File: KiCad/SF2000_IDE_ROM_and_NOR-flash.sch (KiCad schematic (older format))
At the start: 3 parts, among them J5 IDE_ATA_44pin, U13 SST39LF040, U14 SST39LF802C

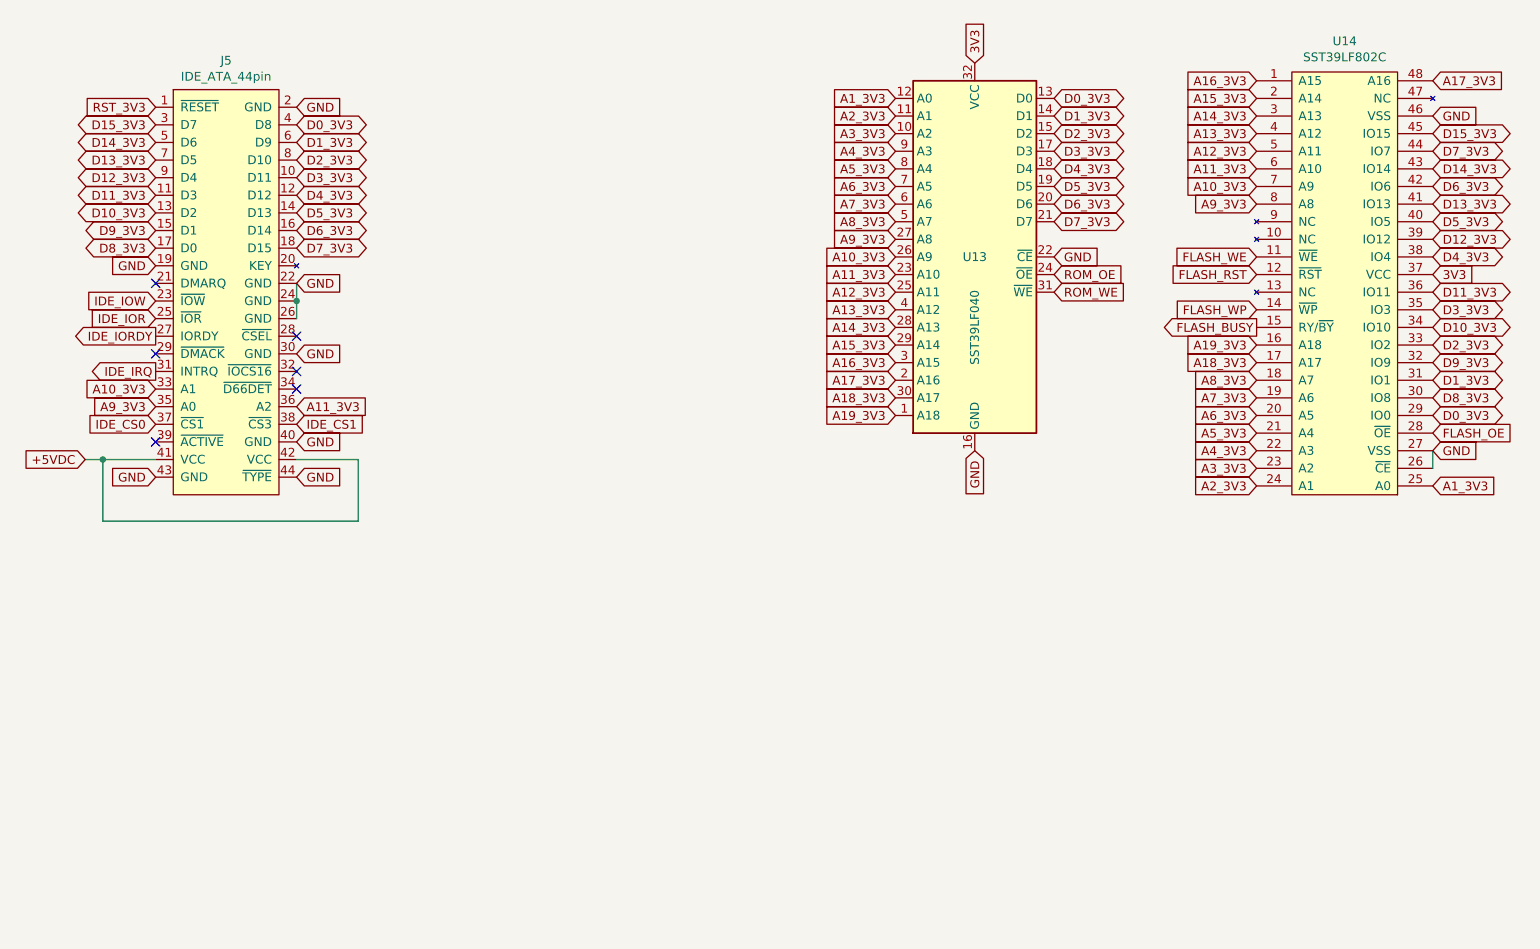
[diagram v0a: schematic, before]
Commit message: added buffering for IDE, rearranged components a bit and did more routing
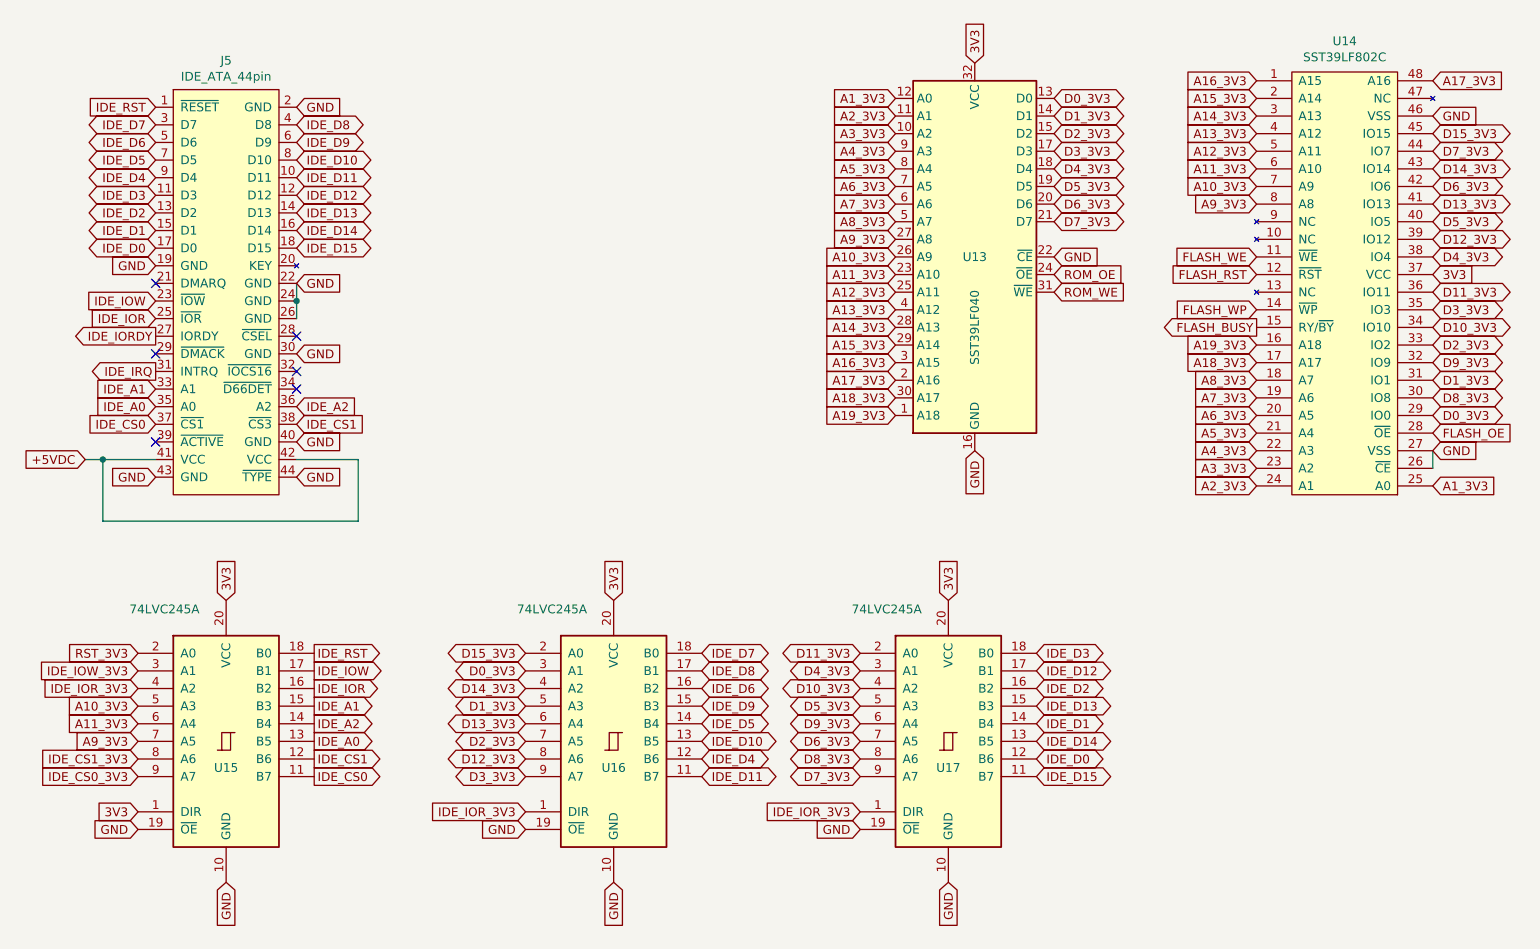
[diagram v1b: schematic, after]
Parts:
- added U15, U16, U17: 74LVC245A, Package_SO:TSSOP-20_4.4x6.5mm_P0.65mm, symbol SF2000:74LVC245A
- J5: footprint Connector_PinSocket_2.00mm:PinSocket_2x22_P2.00mm_Horizontal -> SF2000:PinHeader_2x22_P2.00mm_Vertical
- U13: footprint Package_LCC:PLCC-32_11.4x14.0mm_P1.27mm -> SF2000:PLCC-32_11.4x14.0mm_P1.27mm
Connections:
- net 3V3: now also U15.1 (DIR), U15.20 (VCC), U16.20 (VCC), U17.20 (VCC)
- net A10_3V3: now also U15.5 (A3); no longer J5.33 (A1)
- net A11_3V3: now also U15.6 (A4); no longer J5.36 (A2)
- net A9_3V3: now also U15.7 (A5); no longer J5.35 (A0)
- net D0_3V3: now also U16.3 (A1); no longer J5.4 (D8)
- net D10_3V3: now also U17.4 (A2); no longer J5.13 (D2)
- net D11_3V3: now also U17.2 (A0); no longer J5.11 (D3)
- net D12_3V3: now also U16.8 (A6); no longer J5.9 (D4)
- net D13_3V3: now also U16.6 (A4); no longer J5.7 (D5)
- net D14_3V3: now also U16.4 (A2); no longer J5.5 (D6)
- net D15_3V3: now also U16.2 (A0); no longer J5.3 (D7)
- net D1_3V3: now also U16.5 (A3); no longer J5.6 (D9)
- net D2_3V3: now also U16.7 (A5); no longer J5.8 (D10)
- net D3_3V3: now also U16.9 (A7); no longer J5.10 (D11)
- net D4_3V3: now also U17.3 (A1); no longer J5.12 (D12)
- net D5_3V3: now also U17.5 (A3); no longer J5.14 (D13)
- net D6_3V3: now also U17.7 (A5); no longer J5.16 (D14)
- net D7_3V3: now also U17.9 (A7); no longer J5.18 (D15)
- net D8_3V3: now also U17.8 (A6); no longer J5.17 (D0)
- net D9_3V3: now also U17.6 (A4); no longer J5.15 (D1)
- net GND: now also U15.10 (GND), U15.19 (~OE), U16.10 (GND), U16.19 (~OE), U17.10 (GND), U17.19 (~OE)
- net IDE_CS0: now also U15.11 (B7)
- net IDE_CS1: now also U15.12 (B6)
- net IDE_IOR: now also U15.16 (B2)
- net IDE_IOW: now also U15.17 (B1)
- net RST_3V3: now also U15.2 (A0); no longer J5.1 (~RESET)
- new net IDE_A0: J5.35 (A0), U15.13 (B5)
- new net IDE_A1: J5.33 (A1), U15.15 (B3)
- new net IDE_A2: J5.36 (A2), U15.14 (B4)
- new net IDE_CS0_3V3: U15.9 (A7)
- new net IDE_CS1_3V3: U15.8 (A6)
- new net IDE_D0: J5.17 (D0), U17.12 (B6)
- new net IDE_D1: J5.15 (D1), U17.14 (B4)
- new net IDE_D10: J5.8 (D10), U16.13 (B5)
- new net IDE_D11: J5.10 (D11), U16.11 (B7)
- new net IDE_D12: J5.12 (D12), U17.17 (B1)
- new net IDE_D13: J5.14 (D13), U17.15 (B3)
- new net IDE_D14: J5.16 (D14), U17.13 (B5)
- new net IDE_D15: J5.18 (D15), U17.11 (B7)
- new net IDE_D2: J5.13 (D2), U17.16 (B2)
- new net IDE_D3: J5.11 (D3), U17.18 (B0)
- new net IDE_D4: J5.9 (D4), U16.12 (B6)
- new net IDE_D5: J5.7 (D5), U16.14 (B4)
- new net IDE_D6: J5.5 (D6), U16.16 (B2)
- new net IDE_D7: J5.3 (D7), U16.18 (B0)
- new net IDE_D8: J5.4 (D8), U16.17 (B1)
- new net IDE_D9: J5.6 (D9), U16.15 (B3)
- new net IDE_IOR_3V3: U15.4 (A2), U16.1 (DIR), U17.1 (DIR)
- new net IDE_IOW_3V3: U15.3 (A1)
- new net IDE_RST: J5.1 (~RESET), U15.18 (B0)
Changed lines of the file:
@@
 F 0 "J5" H 2700 4015 50  0000 C CNN
 F 1 "IDE_ATA_44pin" H 2700 3924 50  0000 C CNN
-F 2 "Connector_PinSocket_2.00mm:PinSocket_2x22_P2.00mm_Horizontal" H 2700 2800 50  0001 C CNN
+F 2 "SF2000:PinHeader_2x22_P2.00mm_Vertical" H 2700 2800 50  0001 C CNN
 F 3 "" H 2700 2800 50  0001 C CNN
 	1    2700 2750
@@
 F 0 "U13" H 6950 2600 50  0000 C CNN
 F 1 "SST39LF040" V 6950 2200 50  0000 C CNN
-F 2 "Package_LCC:PLCC-32_11.4x14.0mm_P1.27mm" H 6950 2600 50  0001 C CNN
+F 2 "SF2000:PLCC-32_11.4x14.0mm_P1.27mm" H 6950 2600 50  0001 C CNN
 F 3 "https://ww1.microchip.com/downloads/en/DeviceDoc/20005023B.pdf" H 6950 2700 50  0001 C CNN
 	1    6950 2600
@@
 Text GLabel 7400 2400 2    50   BiDi ~ 0
 D7_3V3
-Text GLabel 3100 1850 2    50   BiDi ~ 0
+Text GLabel 4400 4950 0    50   BiDi ~ 0
 D0_3V3
-Text GLabel 3100 1950 2    50   BiDi ~ 0
+Text GLabel 4400 5150 0    50   BiDi ~ 0
 D1_3V3
-Text GLabel 3100 2050 2    50   BiDi ~ 0
+Text GLabel 4400 5350 0    50   BiDi ~ 0
 D2_3V3
-Text GLabel 3100 2150 2    50   BiDi ~ 0
+Text GLabel 4400 5550 0    50   BiDi ~ 0
 D3_3V3
-Text GLabel 3100 2250 2    50   BiDi ~ 0
+Text GLabel 6300 4950 0    50   BiDi ~ 0
 D4_3V3
-Text GLabel 3100 2350 2    50   BiDi ~ 0
+Text GLabel 6300 5150 0    50   BiDi ~ 0
 D5_3V3
-Text GLabel 3100 2450 2    50   BiDi ~ 0
+Text GLabel 6300 5350 0    50   BiDi ~ 0
 D6_3V3
-Text GLabel 3100 2550 2    50   BiDi ~ 0
+Text GLabel 6300 5550 0    50   BiDi ~ 0
 D7_3V3
-Text GLabel 2300 2550 0    50   BiDi ~ 0
+Text GLabel 6300 5450 0    50   BiDi ~ 0
 D8_3V3
-Text GLabel 2300 2450 0    50   BiDi ~ 0
+Text GLabel 6300 5250 0    50   BiDi ~ 0
 D9_3V3
-Text GLabel 2300 2350 0    50   BiDi ~ 0
+Text GLabel 6300 5050 0    50   BiDi ~ 0
 D10_3V3
-Text GLabel 2300 2250 0    50   BiDi ~ 0
+Text GLabel 6300 4850 0    50   BiDi ~ 0
 D11_3V3
-Text GLabel 2300 2150 0    50   BiDi ~ 0
+Text GLabel 4400 5450 0    50   BiDi ~ 0
 D12_3V3
-Text GLabel 2300 2050 0    50   BiDi ~ 0
+Text GLabel 4400 5250 0    50   BiDi ~ 0
 D13_3V3
-Text GLabel 2300 1950 0    50   BiDi ~ 0
+Text GLabel 4400 5050 0    50   BiDi ~ 0
 D14_3V3
-Text GLabel 2300 1850 0    50   BiDi ~ 0
+Text GLabel 4400 4850 0    50   BiDi ~ 0
 D15_3V3
-Text GLabel 2300 1750 0    50   Input ~ 0
+Text GLabel 2200 4850 0    50   Input ~ 0
 RST_3V3
 Text GLabel 2300 2650 0    50   Input ~ 0
@@
 Text GLabel 2300 3250 0    50   Output ~ 0
 IDE_IRQ
-Text GLabel 2300 3350 0    50   Input ~ 0
+Text GLabel 2200 5150 0    50   Input ~ 0
 A10_3V3
-Text GLabel 2300 3450 0    50   Input ~ 0
+Text GLabel 2200 5350 0    50   Input ~ 0
 A9_3V3
-Text GLabel 3100 3450 2    50   Input ~ 0
+Text GLabel 2200 5250 0    50   Input ~ 0
 A11_3V3
 Text GLabel 3100 3150 2    50   Input ~ 0
@@
 NoConn ~ 3100 3250
 NoConn ~ 3100 3350
+$Comp
+L SF2000:74LVC245A U15
+U 1 1 628D607F
+P 2700 5350
+F 0 "U15" H 2700 5200 50  0000 C CNN
+F 1 "74LVC245A" H 2350 6100 50  0000 C CNN
+F 2 "Package_SO:TSSOP-20_4.4x6.5mm_P0.65mm" H 2700 5350 50  0001 C CNN
+F 3 "http://www.ti.com/lit/gpn/sn74HC245" H 2700 5350 50  0001 C CNN
+	1    2700 5350
+	1    0    0    -1
+$EndComp
+Text GLabel 2700 4550 1    50   Input ~ 0
+3V3
+Text GLabel 2700 6150 3    50   Input ~ 0
+GND
+Text GLabel 2200 5750 0    50   Input ~ 0
+3V3
+Text GLabel 2200 5850 0    50   Input ~ 0
+GND
+Text GLabel 3200 4850 2    50   Output ~ 0
+IDE_RST
+Text GLabel 2300 1750 0    50   Input ~ 0
+IDE_RST
+Text GLabel 2200 4950 0    50   Input ~ 0
+IDE_IOW_3V3
+Text GLabel 3200 4950 2    50   Output ~ 0
+IDE_IOW
+Text GLabel 2200 5050 0    50   Input ~ 0
+IDE_IOR_3V3
+Text GLabel 3200 5050 2    50   Output ~ 0
+IDE_IOR
+Text GLabel 3200 5150 2    50   Output ~ 0
+IDE_A1
+Text GLabel 2300 3350 0    50   Input ~ 0
+IDE_A1
+Text GLabel 3200 5250 2    50   Output ~ 0
+IDE_A2
+Text GLabel 3200 5350 2    50   Output ~ 0
+IDE_A0
+Text GLabel 3100 3450 2    50   Input ~ 0
+IDE_A2
+Text GLabel 2300 3450 0    50   Input ~ 0
+IDE_A0
+Text GLabel 2200 5450 0    50   Input ~ 0
+IDE_CS1_3V3
+Text GLabel 3200 5450 2    50   Output ~ 0
+IDE_CS1
+Text GLabel 2200 5550 0    50   Input ~ 0
+IDE_CS0_3V3
+Text GLabel 3200 5550 2    50   Output ~ 0
+IDE_CS0
+$Comp
+L SF2000:74LVC245A U16
+U 1 1 628E9EE2
+P 4900 5350
+F 0 "U16" H 4900 5200 50  0000 C CNN
+F 1 "74LVC245A" H 4550 6100 50  0000 C CNN
+F 2 "Package_SO:TSSOP-20_4.4x6.5mm_P0.65mm" H 4900 5350 50  0001 C CNN
+F 3 "http://www.ti.com/lit/gpn/sn74HC245" H 4900 5350 50  0001 C CNN
+	1    4900 5350
+	1    0    0    -1
+$EndComp
+Text GLabel 4900 4550 1    50   Input ~ 0
+3V3
+Text GLabel 4900 6150 3    50   Input ~ 0
+GND
+Text GLabel 4400 5850 0    50   Input ~ 0
+GND
+$Comp
+L SF2000:74LVC245A U17
+U 1 1 628ED6C8
+P 6800 5350
+F 0 "U17" H 6800 5200 50  0000 C CNN
+F 1 "74LVC245A" H 6450 6100 50  0000 C CNN
+F 2 "Package_SO:TSSOP-20_4.4x6.5mm_P0.65mm" H 6800 5350 50  0001 C CNN
+F 3 "http://www.ti.com/lit/gpn/sn74HC245" H 6800 5350 50  0001 C CNN
+	1    6800 5350
+	1    0    0    -1
+$EndComp
+Text GLabel 6800 4550 1    50   Input ~ 0
+3V3
+Text GLabel 6800 6150 3    50   Input ~ 0
+GND
+Text GLabel 6300 5850 0    50   Input ~ 0
+GND
+Text GLabel 6300 5750 0    50   Input ~ 0
+IDE_IOR_3V3
+Text GLabel 4400 5750 0    50   Input ~ 0
+IDE_IOR_3V3
+Text GLabel 5400 4850 2    50   BiDi ~ 0
+IDE_D7
+Text GLabel 2300 1850 0    50   BiDi ~ 0
+IDE_D7
+Text GLabel 5400 4950 2    50   BiDi ~ 0
+IDE_D8
+Text GLabel 3100 1850 2    50   BiDi ~ 0
+IDE_D8
+Text GLabel 5400 5050 2    50   BiDi ~ 0
+IDE_D6
+Text GLabel 2300 1950 0    50   BiDi ~ 0
+IDE_D6
+Text GLabel 5400 5150 2    50   BiDi ~ 0
+IDE_D9
+Text GLabel 3100 1950 2    50   BiDi ~ 0
+IDE_D9
+Text GLabel 5400 5250 2    50   BiDi ~ 0
+IDE_D5
+Text GLabel 2300 2050 0    50   BiDi ~ 0
+IDE_D5
+Text GLabel 5400 5350 2    50   BiDi ~ 0
+IDE_D10
+Text GLabel 3100 2050 2    50   BiDi ~ 0
+IDE_D10
+Text GLabel 5400 5450 2    50   BiDi ~ 0
+IDE_D4
+Text GLabel 2300 2150 0    50   BiDi ~ 0
+IDE_D4
+Text GLabel 5400 5550 2    50   BiDi ~ 0
+IDE_D11
+Text GLabel 3100 2150 2    50   BiDi ~ 0
+IDE_D11
+Text GLabel 7300 4850 2    50   BiDi ~ 0
+IDE_D3
+Text GLabel 2300 2250 0    50   BiDi ~ 0
+IDE_D3
+Text GLabel 7300 4950 2    50   BiDi ~ 0
+IDE_D12
+Text GLabel 3100 2250 2    50   BiDi ~ 0
+IDE_D12
+Text GLabel 7300 5050 2    50   BiDi ~ 0
+IDE_D2
+Text GLabel 2300 2350 0    50   BiDi ~ 0
+IDE_D2
+Text GLabel 7300 5150 2    50   BiDi ~ 0
+IDE_D13
+Text GLabel 3100 2350 2    50   BiDi ~ 0
+IDE_D13
+Text GLabel 7300 5250 2    50   BiDi ~ 0
+IDE_D1
+Text GLabel 2300 2450 0    50   BiDi ~ 0
+IDE_D1
+Text GLabel 7300 5350 2    50   BiDi ~ 0
+IDE_D14
+Text GLabel 3100 2450 2    50   BiDi ~ 0
+IDE_D14
+Text GLabel 7300 5450 2    50   BiDi ~ 0
+IDE_D0
+Text GLabel 2300 2550 0    50   BiDi ~ 0
+IDE_D0
+Text GLabel 7300 5550 2    50   BiDi ~ 0
+IDE_D15
+Text GLabel 3100 2550 2    50   BiDi ~ 0
+IDE_D15
 $EndSCHEMATC

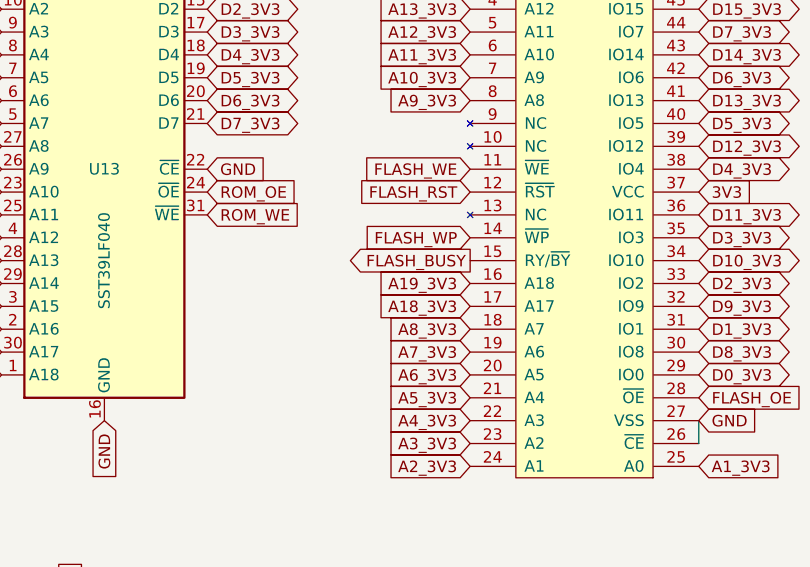
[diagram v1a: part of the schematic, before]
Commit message: more routing and pin assignments done to FPGA
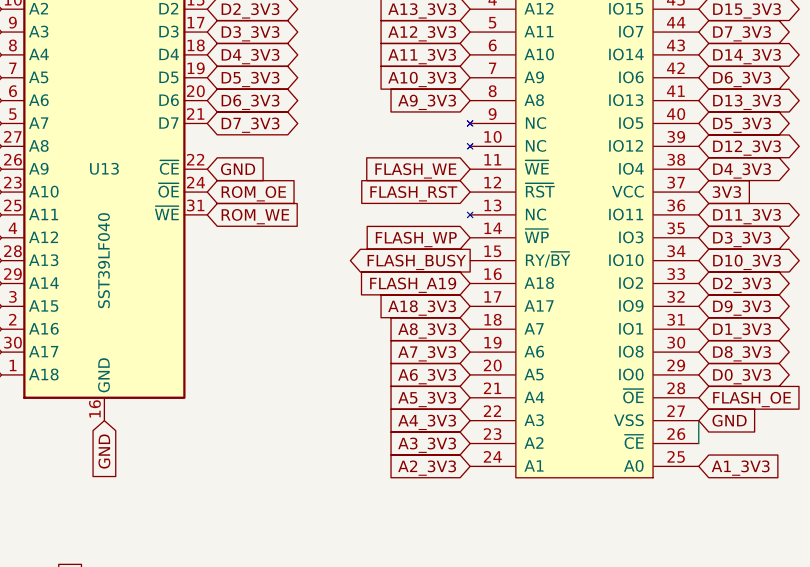
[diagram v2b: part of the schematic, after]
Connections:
- net A19_3V3: no longer U14.16 (A18)
- new net FLASH_A19: U14.16 (A18)
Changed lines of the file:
@@
 A18_3V3
 Text GLabel 8550 3100 0    50   Input ~ 0
-A19_3V3
+FLASH_A19
 Text GLabel 9550 1800 2    50   Input ~ 0
 GND
